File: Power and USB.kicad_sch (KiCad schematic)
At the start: 6 parts, among them IC4 USBLC6-2SC6, J6 USB4085-GF-A

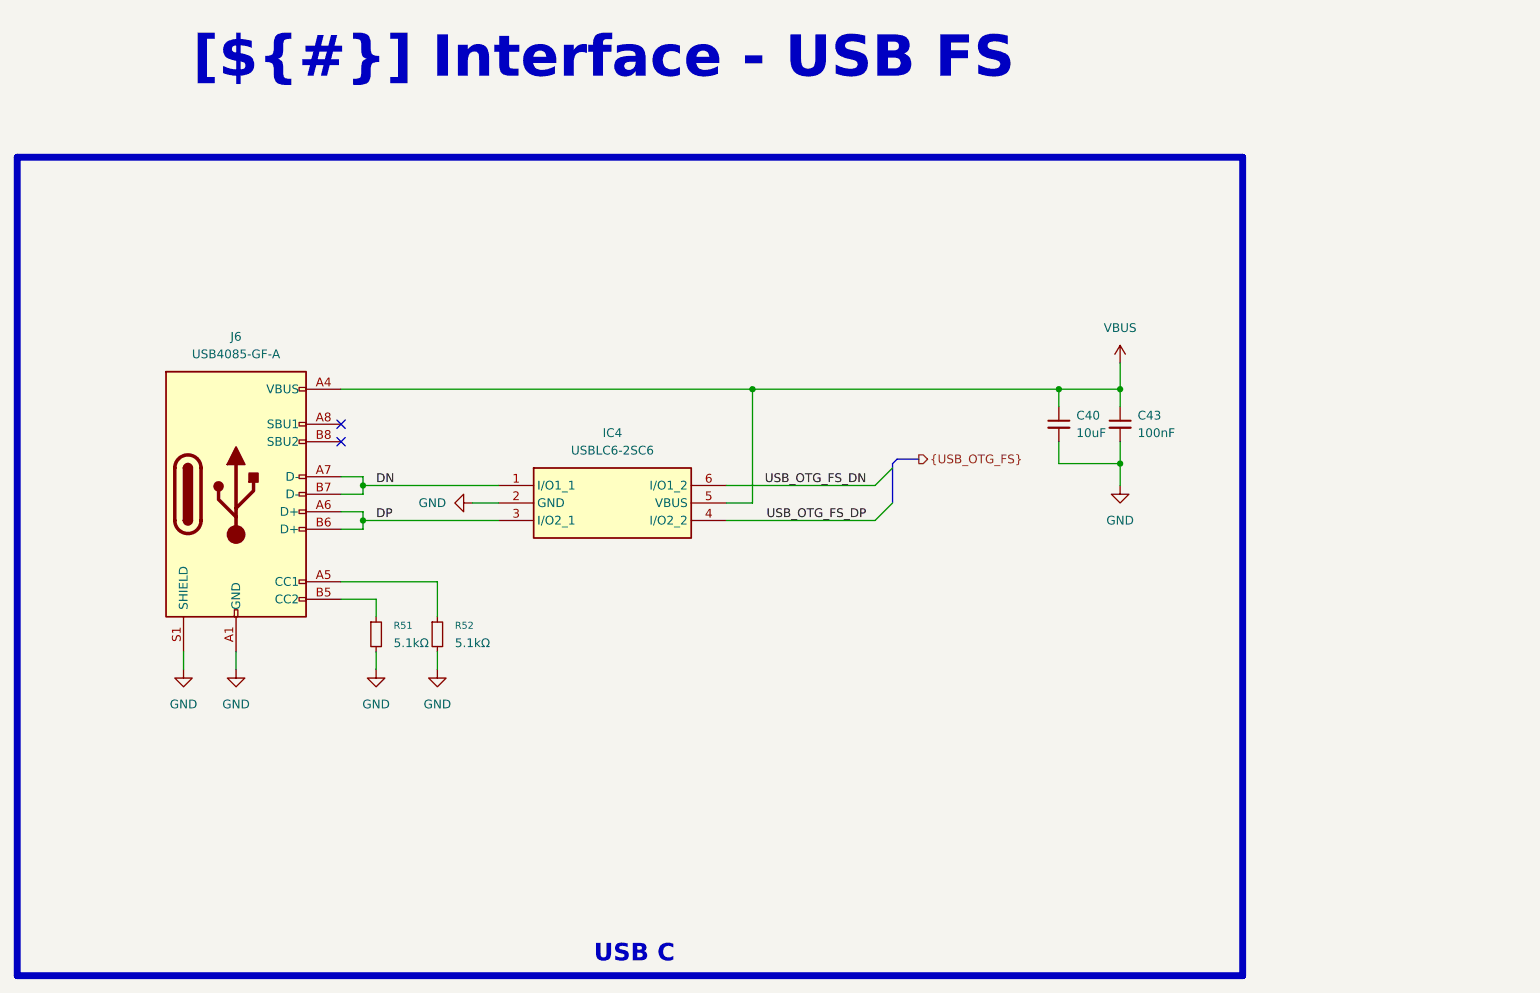
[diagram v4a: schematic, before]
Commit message: added fiducal markers, mounting holes, testpoints
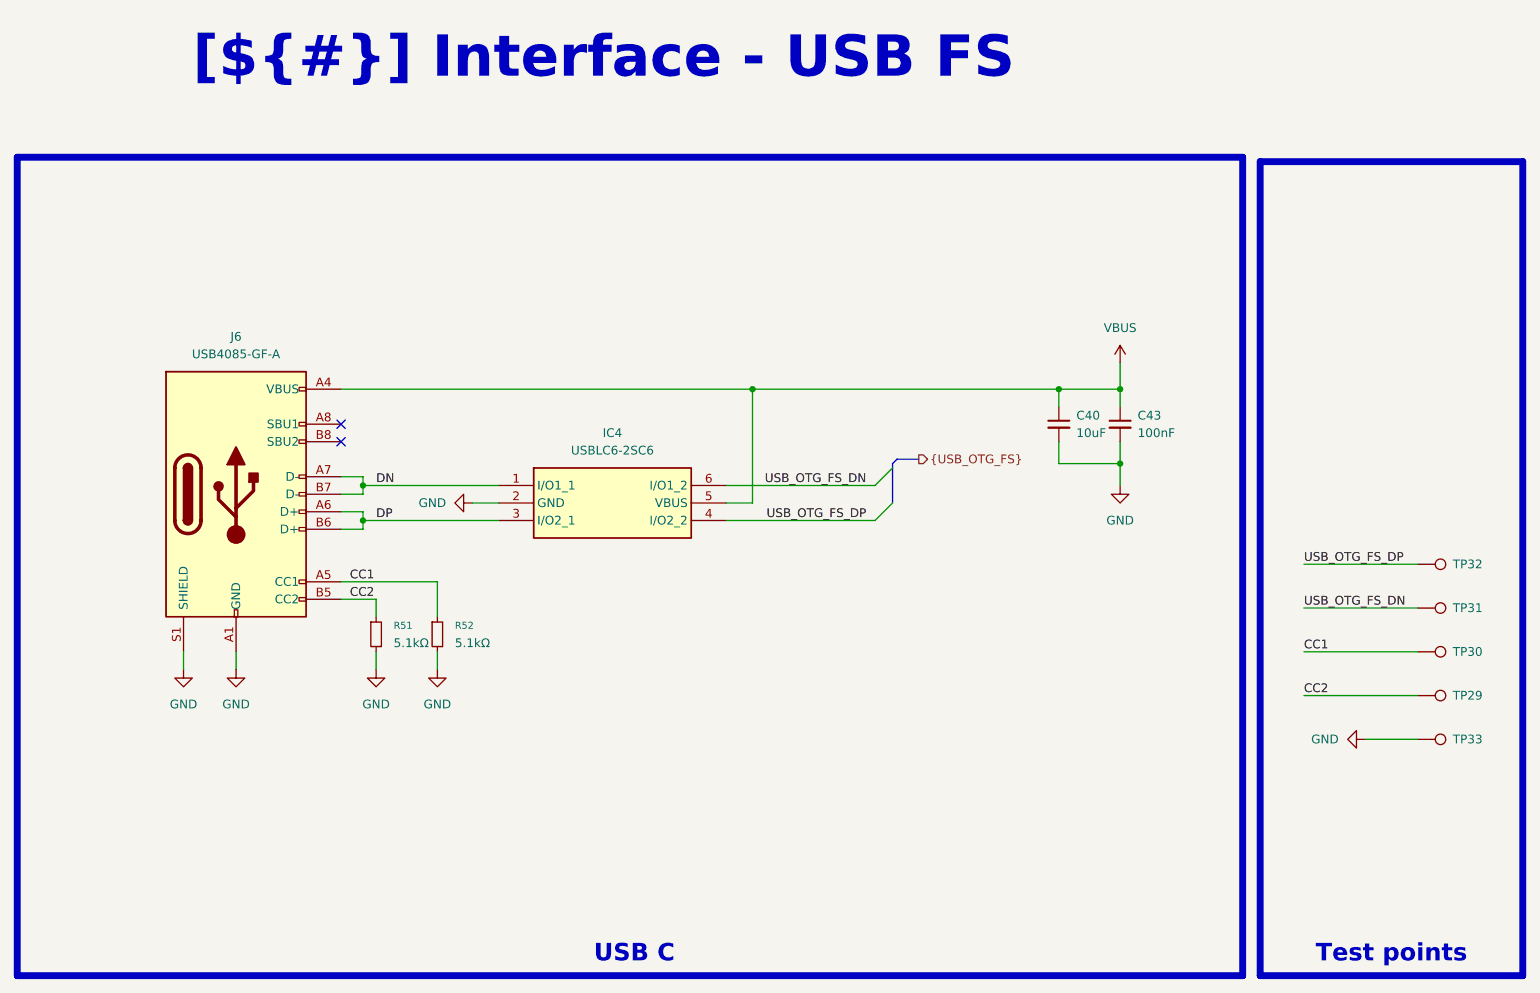
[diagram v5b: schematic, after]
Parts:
- added TP29, TP30, TP31, TP32, TP33: TestPoint, 0_pads:TestPoint_Pad_D0.4mm_Back, symbol Connector:TestPoint
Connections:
- net GND: now also TP33.1
- net USB_OTG_FS_DN: now also TP31.1
- net USB_OTG_FS_DP: now also TP32.1
- net CC1: now reaches J6.A5 (CC1), R52.1
- net CC1: now also TP30.1
- net CC2: now reaches J6.B5 (CC2), R51.1
- net CC2: now also TP29.1

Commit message: test points, colors, drc
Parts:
- TP29, TP30, TP31, TP32, TP33: footprint 0_pads:TestPoint_Pad_D0.4mm_Back -> 0_pads:TestPoint_Pad_D0.5mm_Back
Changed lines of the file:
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@@
 			)
 		)
-		(property "Footprint" "0_pads:TestPoint_Pad_D0.4mm_Back"
+		(property "Footprint" "0_pads:TestPoint_Pad_D0.5mm_Back"
 			(at 266.7 104.14 0)
 			(effects
@@
 			)
 		)
-		(property "Footprint" "0_pads:TestPoint_Pad_D0.4mm_Back"
+		(property "Footprint" "0_pads:TestPoint_Pad_D0.5mm_Back"
 			(at 266.7 110.49 0)
 			(effects
@@
 			)
 		)
-		(property "Footprint" "0_pads:TestPoint_Pad_D0.4mm_Back"
+		(property "Footprint" "0_pads:TestPoint_Pad_D0.5mm_Back"
 			(at 266.7 123.19 0)
 			(effects
@@
 			)
 		)
-		(property "Footprint" "0_pads:TestPoint_Pad_D0.4mm_Back"
+		(property "Footprint" "0_pads:TestPoint_Pad_D0.5mm_Back"
 			(at 266.7 97.79 0)
 			(effects
@@
 			)
 		)
-		(property "Footprint" "0_pads:TestPoint_Pad_D0.4mm_Back"
+		(property "Footprint" "0_pads:TestPoint_Pad_D0.5mm_Back"
 			(at 266.7 116.84 0)
 			(effects

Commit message: fixing drc, generation production files test
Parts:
- added JP2: NC, Jumper:SolderJumper-2_P1.3mm_Open_TrianglePad1.0x1.5mm, symbol 0_modules:Jumper_2_Bridged
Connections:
- net GND: now also JP2.1 (A); no longer J6.S1 (SHIELD)
- new net: J6.S1 (SHIELD), JP2.2 (B)
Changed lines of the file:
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@@
+		)
+	)
+	(wire
+		(pts
+			(xy 87.63 118.11) (xy 87.63 116.84)
+		)
+		(stroke
+			(width 0)
+			(type default)
 		)
 	)
@@
 	(wire
 		(pts
+			(xy 95.25 105.41) (xy 95.25 118.11)
+		)
+		(stroke
+			(width 0)
+			(type default)
+		)
+	)
+	(wire
+		(pts
 			(xy 250.19 99.06) (xy 266.7 99.06)
 		)
@@
 	(wire
 		(pts
-			(xy 95.25 105.41) (xy 95.25 107.95)
-		)
-		(stroke
-			(width 0)
-			(type default)
-		)
-	)
-	(wire
-		(pts
-			(xy 87.63 105.41) (xy 87.63 107.95)
-		)
-		(stroke
-			(width 0)
-			(type default)
-		)
-	)
-	(wire
-		(pts
 			(xy 110.49 67.31) (xy 170.18 67.31)
 		)
@@
 		(pts
 			(xy 115.57 97.79) (xy 115.57 100.33)
+		)
+		(stroke
+			(width 0)
+			(type default)
+		)
+	)
+	(wire
+		(pts
+			(xy 87.63 105.41) (xy 87.63 106.68)
 		)
 		(stroke
@@
 	(symbol
 		(lib_id "power:GND")
-		(at 87.63 107.95 0)
+		(at 87.63 118.11 0)
 		(unit 1)
 		(exclude_from_sim no)
@@
 		(fields_autoplaced yes)
 		(property "Reference" "#PWR097"
-			(at 87.63 114.3 0)
+			(at 87.63 124.46 0)
 			(effects
 				(font
@@
 		)
 		(property "Value" "GND"
-			(at 87.63 113.03 0)
+			(at 87.63 123.19 0)
 			(effects
 				(font
@@
 		)
 		(property "Footprint" ""
-			(at 87.63 107.95 0)
+			(at 87.63 118.11 0)
 			(effects
 				(font
@@
 		)
 		(property "Datasheet" ""
-			(at 87.63 107.95 0)
+			(at 87.63 118.11 0)
 			(effects
 				(font
@@
 		)
 		(property "Description" "Power symbol creates a global label with name \"GND\" , ground"
-			(at 87.63 107.95 0)
+			(at 87.63 118.11 0)
 			(effects
 				(font
@@
 	(symbol
 		(lib_id "power:GND")
-		(at 95.25 107.95 0)
+		(at 95.25 118.11 0)
 		(unit 1)
 		(exclude_from_sim no)
@@
 		(fields_autoplaced yes)
 		(property "Reference" "#PWR096"
-			(at 95.25 114.3 0)
+			(at 95.25 124.46 0)
 			(effects
 				(font
@@
 		)
 		(property "Value" "GND"
-			(at 95.25 113.03 0)
+			(at 95.25 123.19 0)
 			(effects
 				(font
@@
 		)
 		(property "Footprint" ""
-			(at 95.25 107.95 0)
+			(at 95.25 118.11 0)
 			(effects
 				(font
@@
 		)
 		(property "Datasheet" ""
-			(at 95.25 107.95 0)
+			(at 95.25 118.11 0)
 			(effects
 				(font
@@
 		)
 		(property "Description" "Power symbol creates a global label with name \"GND\" , ground"
-			(at 95.25 107.95 0)
+			(at 95.25 118.11 0)
 			(effects
 				(font
@@
 					(unit 1)
 				)
+			)
+		)
+	)
+	(symbol
+		(lib_id "0_modules:Jumper_2_Bridged")
+		(at 87.63 111.76 90)
+		(unit 1)
+		(exclude_from_sim no)
+		(in_bom yes)
+		(on_board yes)
+		(dnp no)
+		(fields_autoplaced yes)
+		(property "Reference" "JP2"
+			(at 88.9 110.49 90)
+			(effects
+				(font
+					(size 1.27 1.27)
+				)
+				(justify right)
+			)
+		)
+		(property "Value" "NC"
+			(at 88.9 113.03 90)
+			(effects
+				(font
+					(size 1.27 1.27)
+				)
+				(justify right)
+			)
+		)
+		(property "Footprint" "Jumper:SolderJumper-2_P1.3mm_Open_TrianglePad1.0x1.5mm"
+			(at 87.63 111.76 0)
+			(effects
+				(font
+					(size 1.27 1.27)
+				)
+				(hide yes)
+			)
+		)
+		(property "Datasheet" "~"
+			(at 87.63 111.76 0)
+			(effects
+				(font
+					(size 1.27 1.27)
+				)
+				(hide yes)
+			)
+		)
+		(property "Description" "Jumper, 2-pole, closed/bridged"
+			(at 87.63 111.76 0)
+			(effects
+				(font
+					(size 1.27 1.27)
+				)
+				(hide yes)
+			)
+		)
+		(pin "1"
+		)
+		(pin "2"
+		)
+		(instances
+			(project "transmitter"
+				(path "/0650c7a8-acba-429c-9f8e-eec0baf0bc1c/fede4c36-00cc-4d3d-b71c-5243ba232202/97a2efac-bb12-4130-96cc-5d19fa63b112"
+					(reference "JP2")
+					(unit 1)
+				)

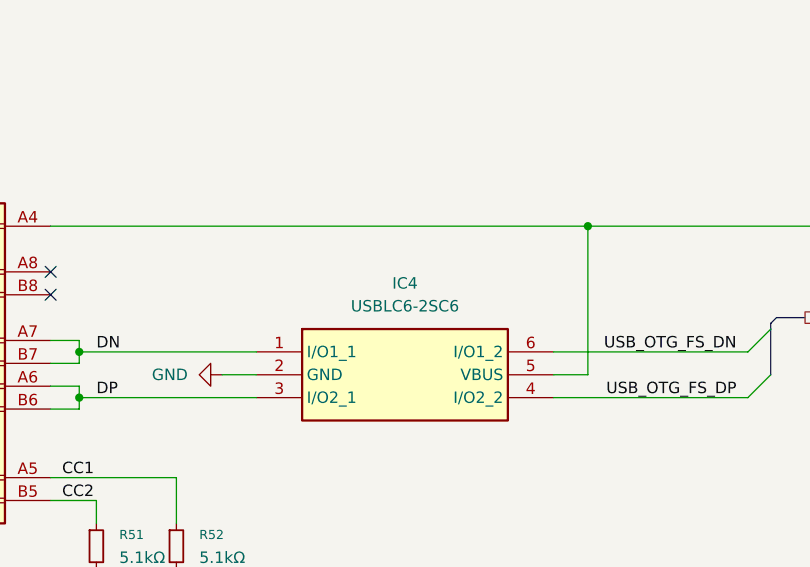
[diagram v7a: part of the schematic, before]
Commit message: designator chagnes and cleanup silkscreen
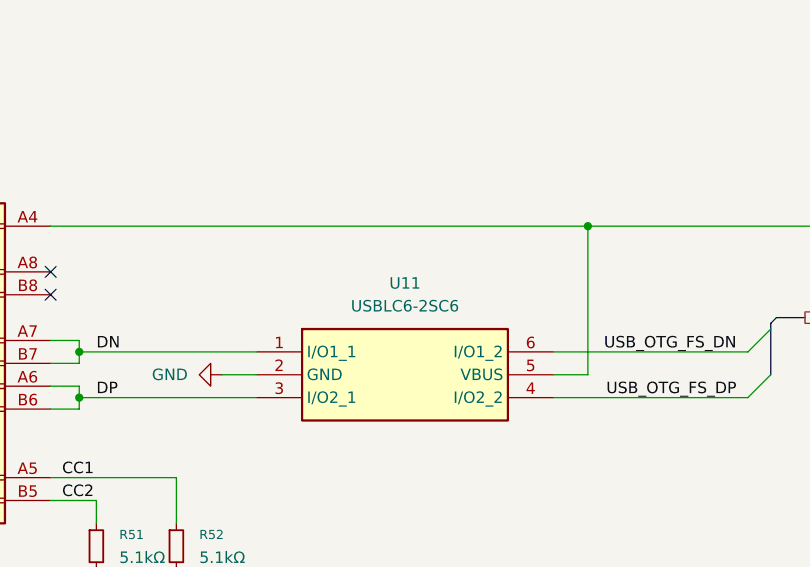
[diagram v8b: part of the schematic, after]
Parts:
- C40: LCSC PN (none) -> C15850
- C43: LCSC PN (none) -> C1525
- J6: LCSC PN (none) -> C7095263
- R51, R52: LCSC PN (none) -> C25905
- U11: renamed from IC4; LCSC PN (none) -> C5180249
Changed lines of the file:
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@@
+			)
+		)
+		(property "LCSC PN" "C25905"
+			(at 124.46 102.87 0)
+			(effects
+				(font
+					(size 1.27 1.27)
+				)
+				(hide yes)
 			)
 		)
@@
 			)
 		)
+		(property "LCSC PN" "C1525"
+			(at 223.52 72.39 0)
+			(effects
+				(font
+					(size 1.27 1.27)
+				)
+				(hide yes)
+			)
+		)
 		(pin "1"
 		)
@@
 			)
 		)
+		(property "LCSC PN" "C15850"
+			(at 214.63 72.39 0)
+			(effects
+				(font
+					(size 1.27 1.27)
+				)
+				(hide yes)
+			)
+		)
 		(pin "2"
 		)
@@
 			)
 		)
+		(property "LCSC PN" "C25905"
+			(at 115.57 102.87 0)
+			(effects
+				(font
+					(size 1.27 1.27)
+				)
+				(hide yes)
+			)
+		)
 		(pin "1"
 		)
@@
 		(dnp no)
 		(fields_autoplaced yes)
-		(property "Reference" "IC4"
+		(property "Reference" "U11"
 			(at 149.86 73.66 0)
 			(effects
@@
 			)
 		)
+		(property "LCSC PN" "C5180249"
+			(at 133.35 81.28 0)
+			(effects
+				(font
+					(size 1.27 1.27)
+				)
+				(hide yes)
+			)
+		)
 		(pin "1"
 		)
@@
 			(project ""
 				(path "/0650c7a8-acba-429c-9f8e-eec0baf0bc1c/fede4c36-00cc-4d3d-b71c-5243ba232202/97a2efac-bb12-4130-96cc-5d19fa63b112"
-					(reference "IC4")
+					(reference "U11")
 					(unit 1)
 				)
@@
 			(at 95.25 82.55 0)
 			(effects
+				(font
+					(size 1.27 1.27)
+				)
+				(hide yes)
+			)
+		)
+		(property "LCSC PN" "C7095263"
+			(at 95.25 82.55 0)
+			(effects
